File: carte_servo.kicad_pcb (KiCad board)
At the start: 4 copper layers, 185 x 106.7 mm, 121 parts, among them J10 Conn_01x03_Male, J11 Transistor_2, J12 Transistor_1, J13 Transistor_4, J14 Transistor_.3, J16 Conn_01x04_Male, J17 Conn_01x04_Male, J18 Conn_01x03_Male, J19 Conn_01x03_Male, J2 Conn_02x04_Top_Bottom, J20 Stepper, J21 Stepper, J24 Conn_LEDs, J25 Conn_AX12, J29 Conn_AX12, J5 Conn_01x03_Male, J6 Conn_01x03_Male, J7 Conn_01x03_Male, J8 Conn_01x03_Male, J9 Conn_01x03_Male, P1 USB_C_Plug_USB2.0, Q1 DMN2011UTS, Q2 DMN2011UTS, Q3 DMN2011UTS, Q4 DMN2011UTS, Q6 DMN2011UTS, Q7 CSD17307Q5A, Q8 CSD17579Q5A, SW1 CK_KMS2xxG, U1 XGZP6897D_differential_pressu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, U2 XGZP6897D_differential_pressu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, U3 TMC2208_SILENTSTEPSTICK, U4 TMC2208_SILENTSTEPSTICK, U5 74LVC2G241, U6 SN65HVD230, U7 LD1117S33TR_SOT223, U8 ESP32-S3-WROOM-1, U9 LM3150MH

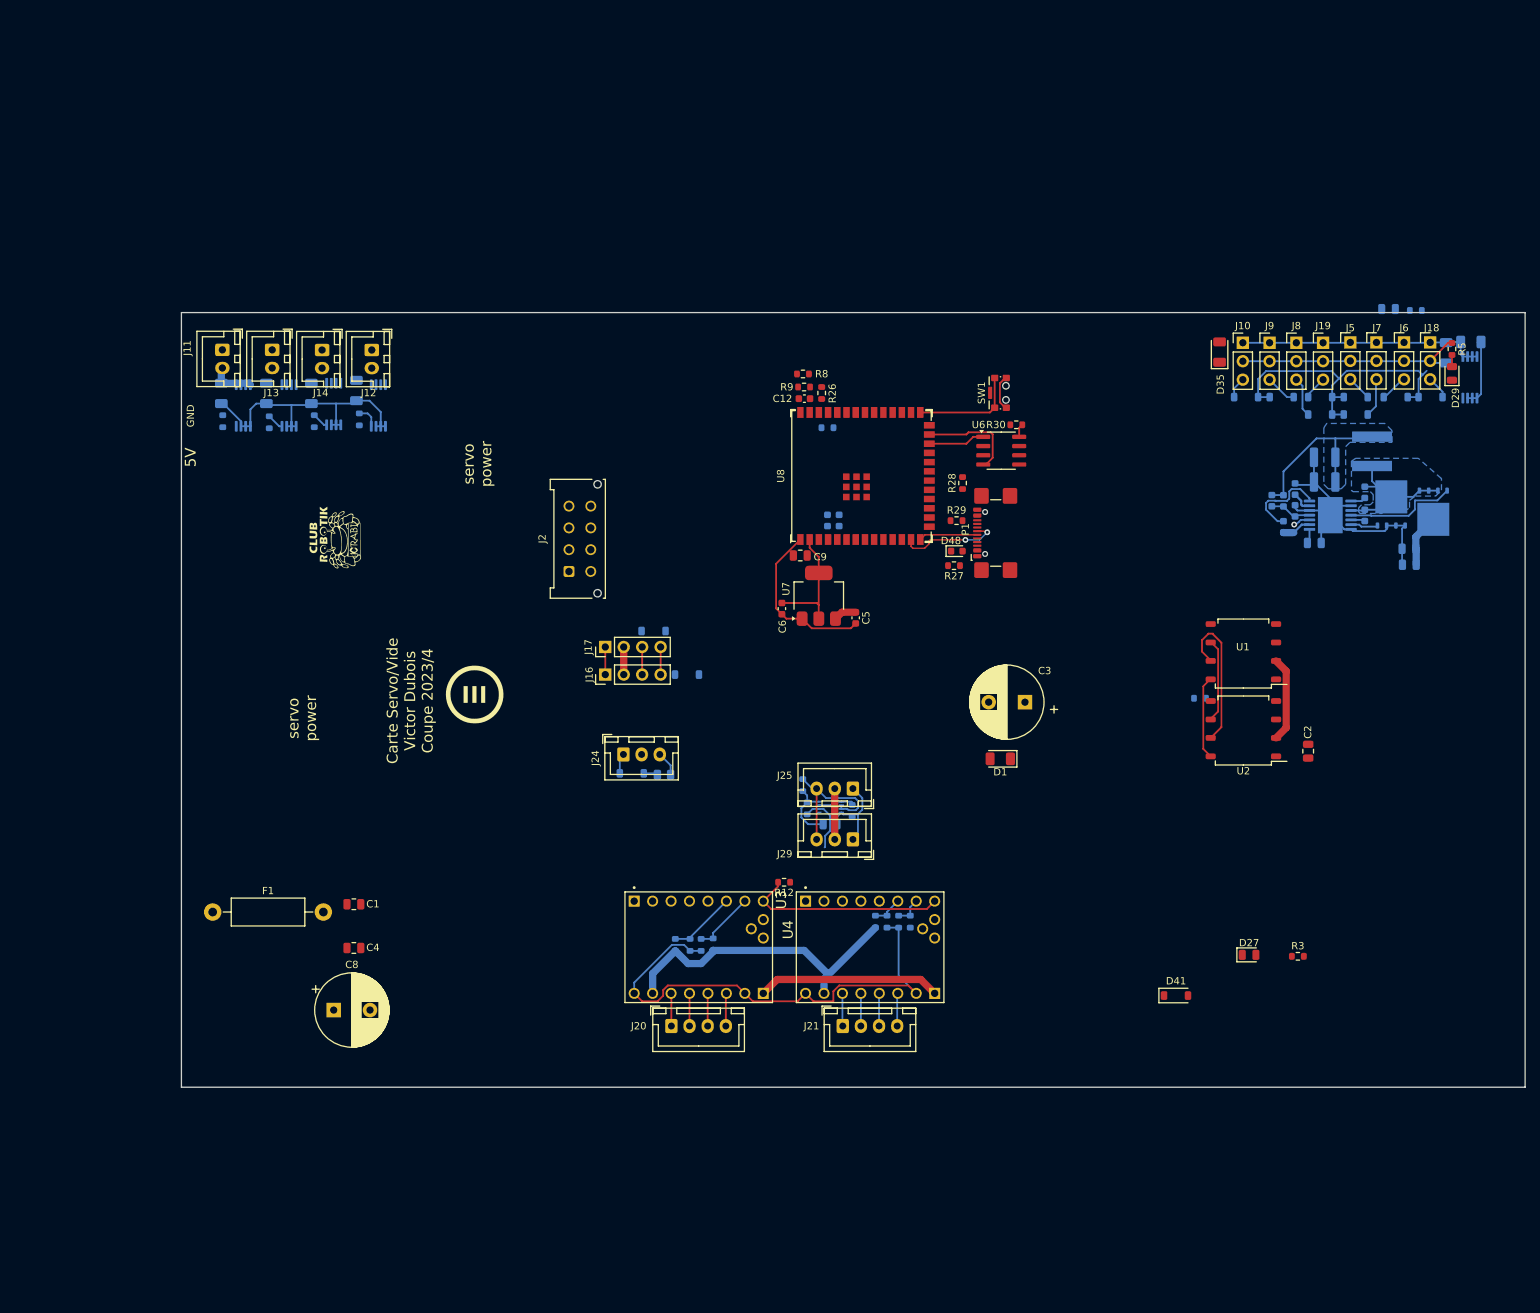
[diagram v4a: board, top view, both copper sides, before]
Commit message: add DCDC 5V
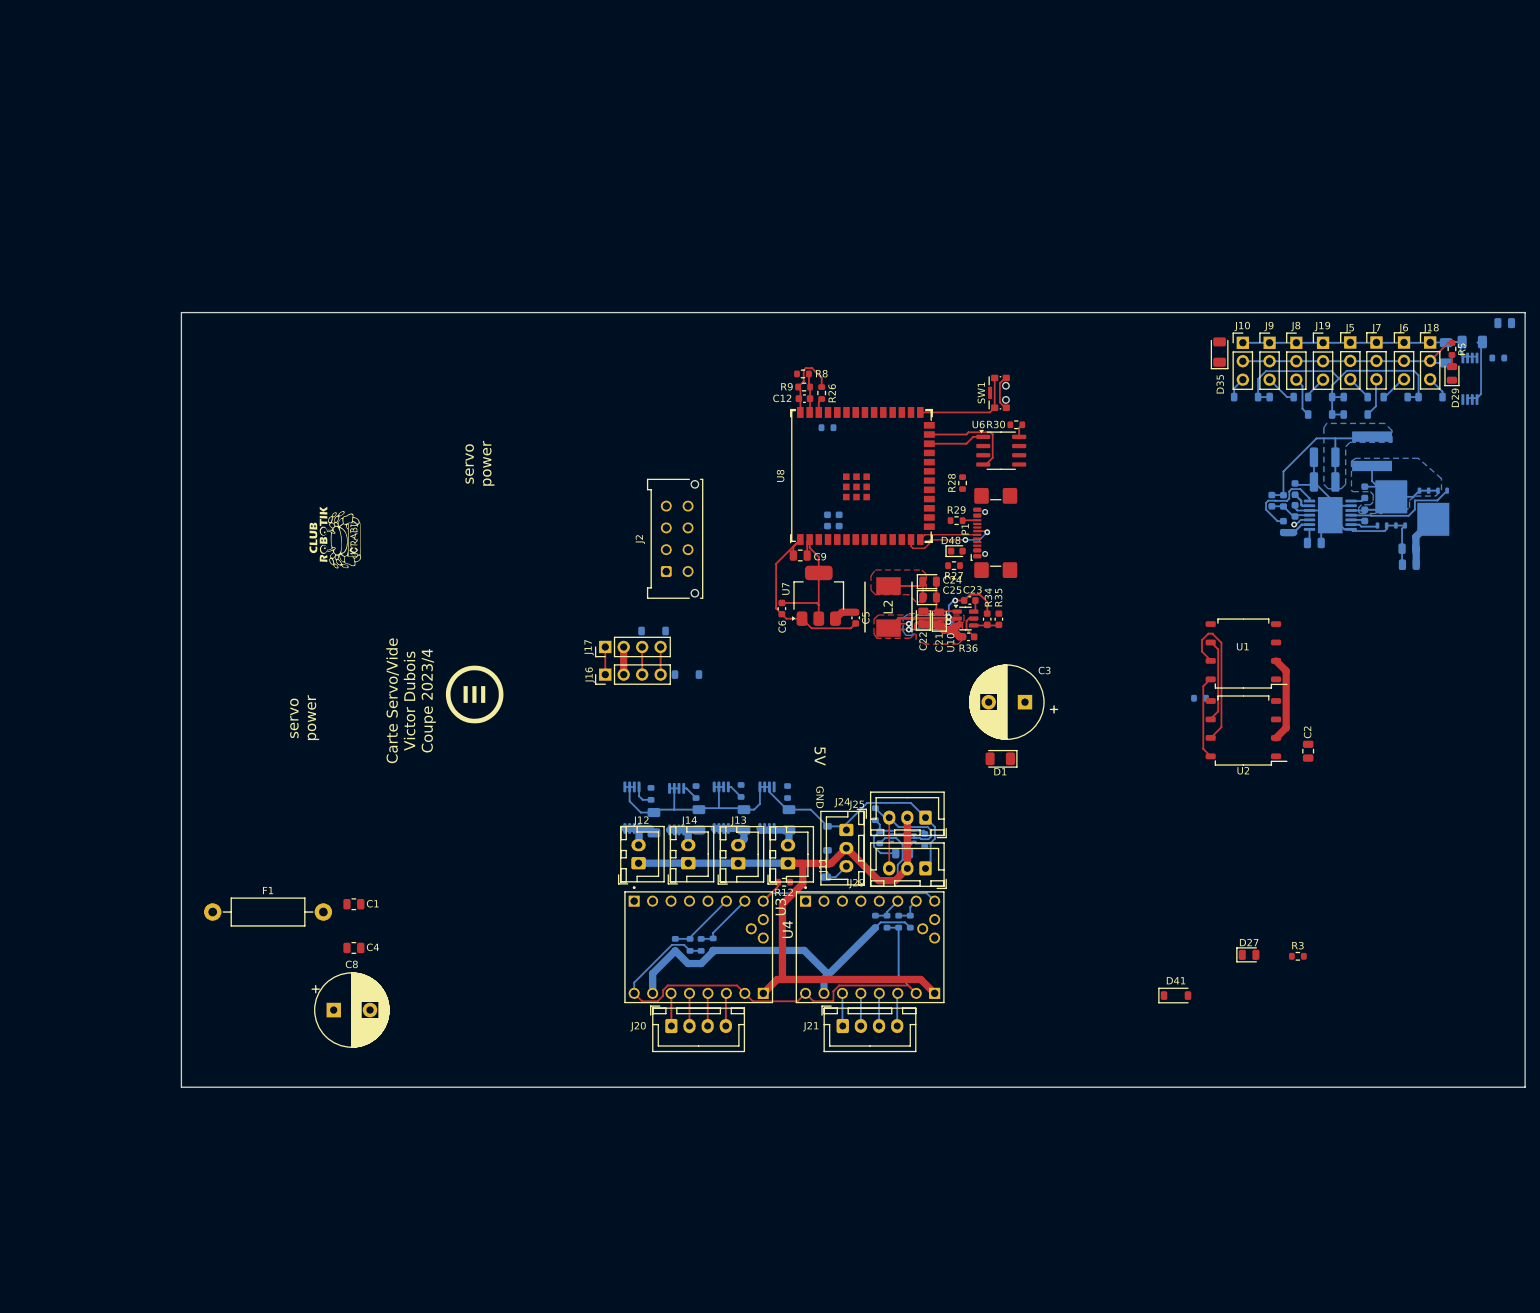
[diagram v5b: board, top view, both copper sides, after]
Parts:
- added C21: 10uF, LED_SMD:LED_0805_2012Metric, F.Cu at (185.4, 100.7)
- added C22: 10uF, LED_SMD:LED_0805_2012Metric, F.Cu at (183.2, 100.6)
- added C23: 100nF, Capacitor_SMD:C_0603_1608Metric, F.Cu at (189.6, 98.2)
- added C24: 22uF, LED_SMD:LED_0805_2012Metric, F.Cu at (184.1, 95.6)
- added C25: 22uF, LED_SMD:LED_0805_2012Metric, F.Cu at (184.1, 97.8)
- added L2: IHLP2525CZER3R3M11, Victor:INDPM6965X300N, F.Cu at (178.4, 99.1)
- added R34: 56.2k, Capacitor_SMD:C_0603_1608Metric, F.Cu at (192.0, 100.8)
- added R35: 10k, Capacitor_SMD:C_0603_1608Metric, F.Cu at (193.6, 100.8)
- added R36: 10k, Capacitor_SMD:C_0603_1608Metric, F.Cu at (189.4, 103.2)
- added U10: TPS563200, Package_TO_SOT_SMD:SOT-23-6, F.Cu at (189.0, 100.7)
- moved J11 105.2 mm to (164.6, 134.4), turned to 90 degrees
- moved D6 97.8 mm to (164.7, 128.4), turned to 90 degrees
- moved J13 95.5 mm to (157.7, 134.4), turned to 90 degrees
- moved R17 93.0 mm to (164.5, 124.6), turned to -90 degrees
- moved Q2 90.9 mm to (161.7, 126.7), turned to -90 degrees
- moved D25 88.2 mm to (158.5, 128.4), turned to 90 degrees
- moved J14 86.8 mm to (150.8, 134.4), turned to 90 degrees
- moved R19 82.5 mm to (158.1, 124.4), turned to -90 degrees
- moved Q4 81.3 mm to (155.4, 126.7), turned to -90 degrees
- moved J12 79.7 mm to (144.0, 134.4), turned to 90 degrees
- moved D7 79.4 mm to (152.3, 128.4), turned to 90 degrees
- moved R20 73.3 mm to (151.9, 124.6), turned to -90 degrees
- moved Q3 73.1 mm to (149.2, 126.9), turned to -90 degrees
- moved D26 72.3 mm to (146.1, 128.8), turned to 90 degrees
- moved Q1 65.5 mm to (143.1, 126.7), turned to -90 degrees
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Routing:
- net BATT_12V: track 43.5 -> 110.2 mm
- net /DCDC_5V/SW_DCDC5V: track 0.00 -> 40.4 mm, vias 0 -> 5
- net GND: track 261.5 -> 301.8 mm
- net 5V: track 71.2 -> 83.3 mm
- net TRANSISTOR_OUT_4: track 0.00 -> 6.61 mm
- net TRANSISTOR_OUT_1: track 0.00 -> 6.56 mm
- net TRANSISTOR_OUT_3: track 0.00 -> 6.22 mm
- net sense_12V: track 0.00 -> 5.39 mm
- net /DCDC_5V/enable: track 0.00 -> 3.75 mm
- net Net-(U10-VFB): track 0.00 -> 3.48 mm
- net 3.3V: track 16.6 -> 19.0 mm
- net Net-(P1-VCONN): track 0.00 -> 2.05 mm
- net sense_5V: track 0.00 -> 2.01 mm
- net Net-(U10-VBST): track 0.00 -> 1.63 mm
- added copper zone on B.Cu, net /DCDC_5V/SW_DCDC5V
- added copper zone on F.Cu, net /DCDC_5V/SW_DCDC5V
- added copper zone on F.Cu, net 5V
- added copper zone on F.Cu, net BATT_12V

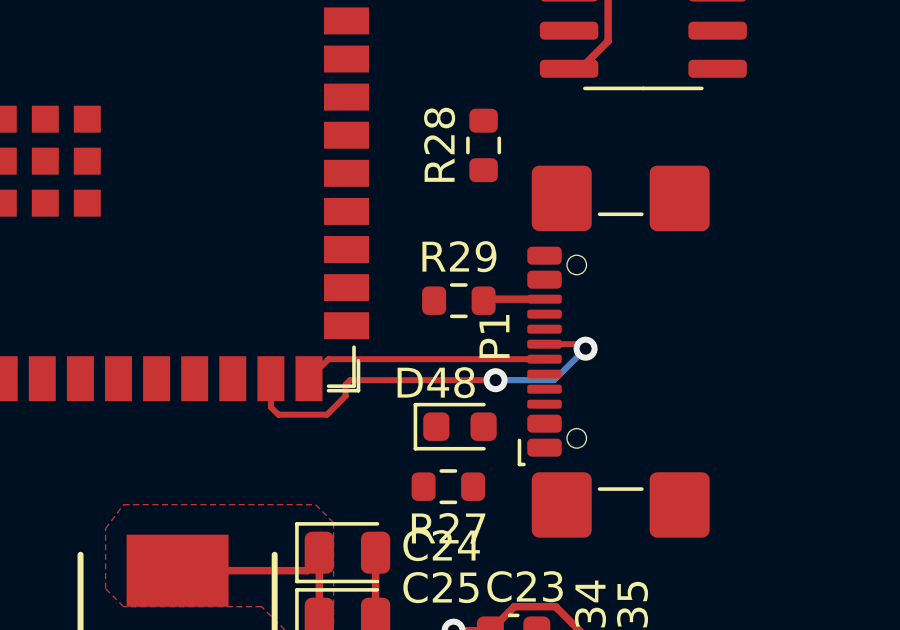
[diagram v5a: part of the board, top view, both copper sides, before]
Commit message: add ESD diodes for USB
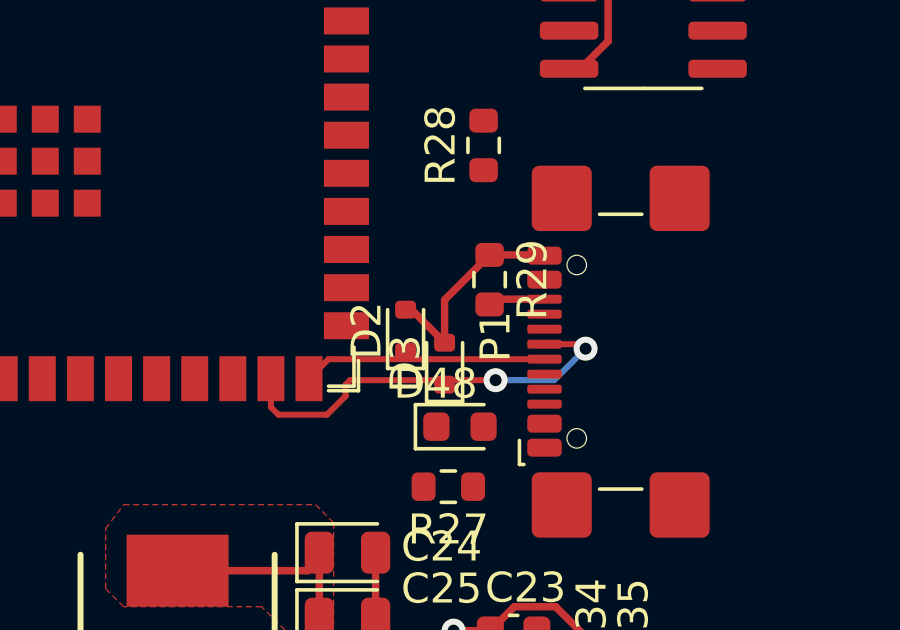
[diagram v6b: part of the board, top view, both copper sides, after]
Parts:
- added D2: ESD321, Diode_SMD:D_SOD-523, F.Cu at (186.0, 88.2)
- added D3: ESD321, Diode_SMD:D_SOD-523, F.Cu at (187.3, 89.3)
- moved R29 1.24 mm to (188.8, 86.5), turned to -90 degrees
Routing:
- net GND: track 301.8 -> 308.9 mm

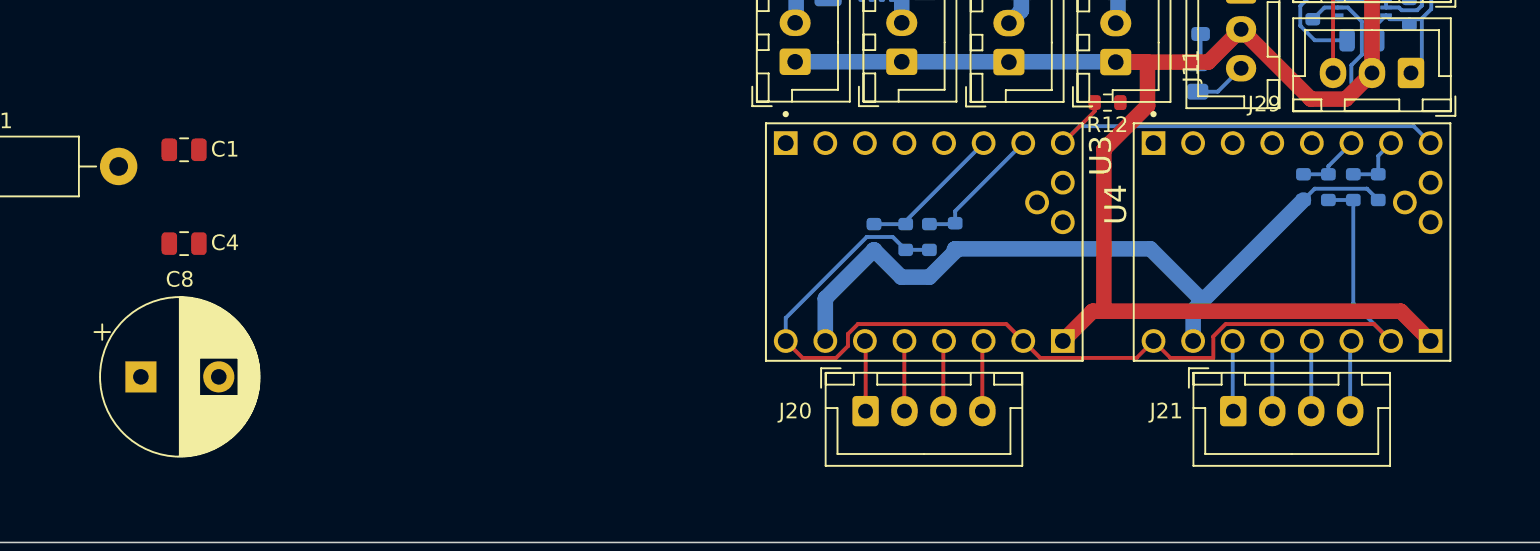
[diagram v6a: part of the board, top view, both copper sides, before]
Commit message: fix warnings + separate enable for Steppers
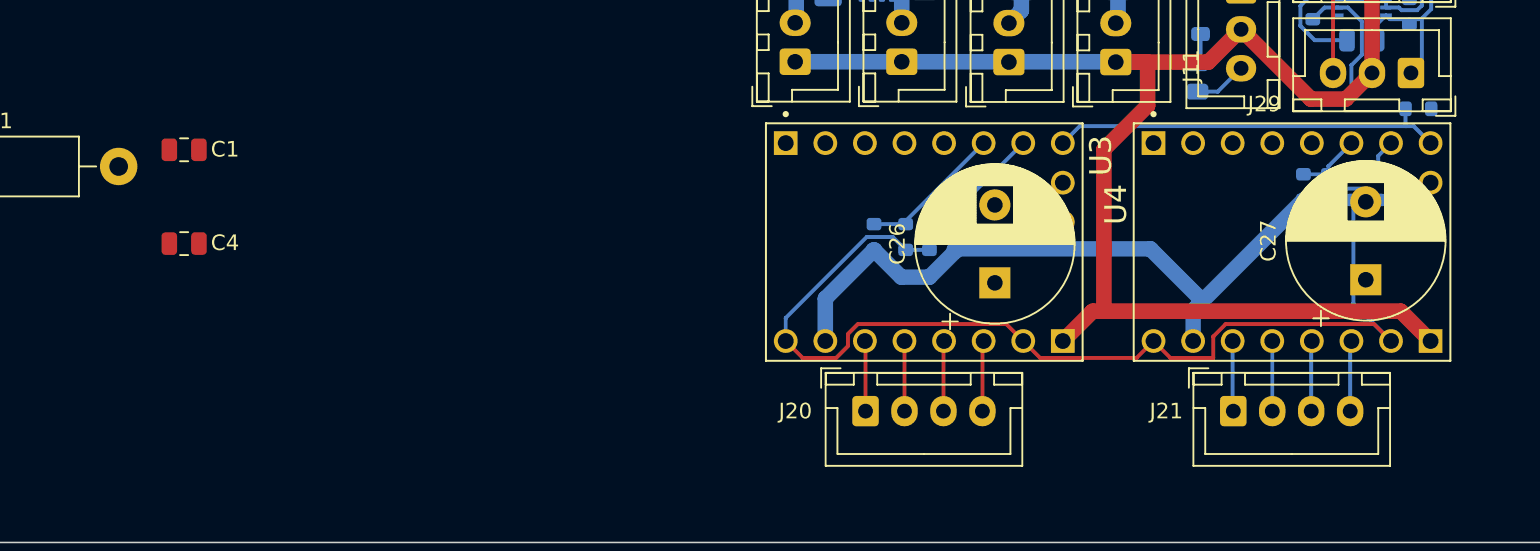
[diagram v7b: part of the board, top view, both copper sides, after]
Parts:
- removed C8: C_Polarized, Capacitor_THT:CP_Radial_D10.0mm_P5.00mm
- added C26: C_Polarized, Capacitor_THT:CP_Radial_D10.0mm_P5.00mm, F.Cu at (156.8, 148.6)
- added C27: C_Polarized, Capacitor_THT:CP_Radial_D10.0mm_P5.00mm, F.Cu at (180.6, 148.4)
- R12: moved to B.Cu
- moved R12 20.0 mm to (184.0, 137.4)
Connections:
- R12 pad 1: ENABLE_SERVO_POWER_2 -> ENABLE_SERVO_POWER_1
- R12 pad 2: ENABLE_SERVO_POWER_1 -> ENABLE_STEPPER_POWER
- R2 pad 1: ENABLE_SERVO_POWER_2 -> ENABLE_SERVO_POWER_1
- U3 pad JP1_8: ENABLE_SERVO_POWER_1 -> ENABLE_STEPPER_POWER
- U4 pad JP1_8: ENABLE_SERVO_POWER_1 -> ENABLE_STEPPER_POWER
- U8 pad 36: ENABLE_SERVO_POWER_2 -> ENABLE_SERVO_POWER_1
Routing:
- net ENABLE_SERVO_POWER_1: track 30.3 -> 2.38 mm
- net ENABLE_STEPPER_POWER: track 0.00 -> 25.6 mm
